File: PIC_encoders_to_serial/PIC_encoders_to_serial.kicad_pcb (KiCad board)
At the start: 4 copper layers, 35 x 35 mm, 20 parts, among them J1 Programming, J2 Conn_01x02, J3 Conn_01x04, J4 Conn_01x05, J5 Conn_01x05, U1 DSPIC33FJ64MC802-xSP, U2 LM78L33_TO92

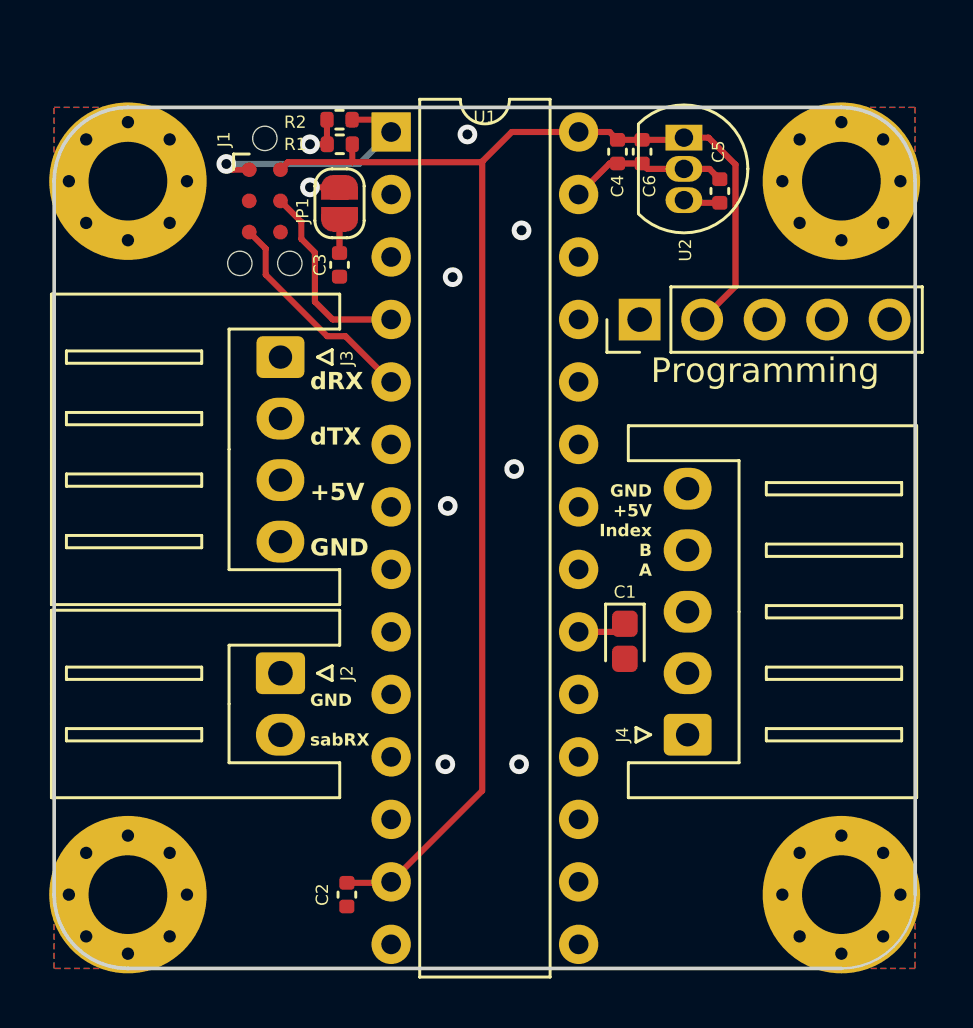
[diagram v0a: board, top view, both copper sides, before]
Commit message: changed connectors from JST XH to Molex mini-SPOX
mini-spox is smaller, but retains an almost 2.54mm pitch, so is still somewhat compatible with pin headers if need be
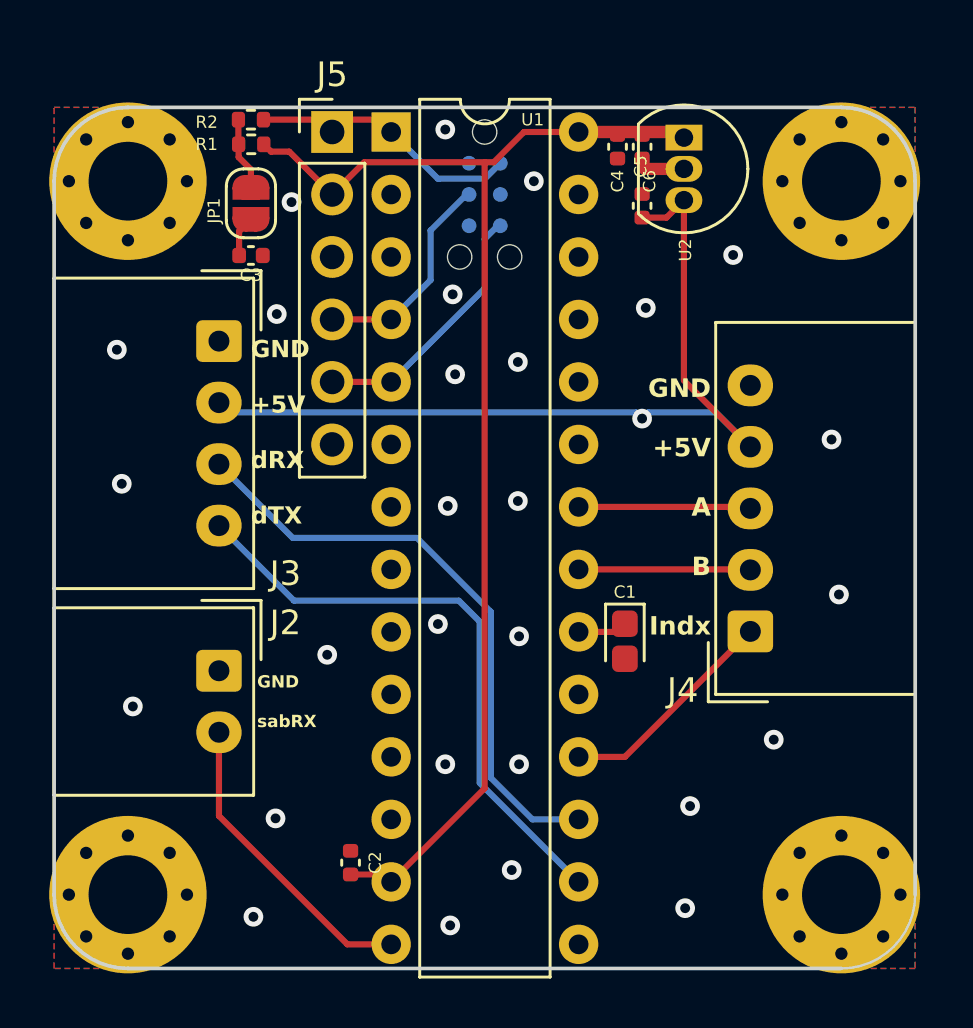
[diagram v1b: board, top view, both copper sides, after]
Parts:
- J1: moved to B.Cu
- J2: footprint Connector_JST:JST_XH_S2B-XH-A_1x02_P2.50mm_Horizontal -> Connector_Molex:Molex_SPOX_5268-02A_1x02_P2.50mm_Horizontal
- J3: footprint Connector_JST:JST_XH_S4B-XH-A_1x04_P2.50mm_Horizontal -> Connector_Molex:Molex_SPOX_5268-04A_1x04_P2.50mm_Horizontal
- J4: footprint Connector_JST:JST_XH_S5B-XH-A_1x05_P2.50mm_Horizontal -> Connector_Molex:Molex_SPOX_5268-05A_1x05_P2.50mm_Horizontal
- J5: value Conn_01x05 -> Programming; footprint Connector_PinHeader_2.54mm:PinHeader_1x05_P2.54mm_Vertical -> Connector_PinHeader_2.54mm:PinHeader_1x06_P2.54mm_Vertical
- moved J5 14.6 mm to (126.3, 56.0), turned to 0 degrees
- moved J1 8.94 mm to (132.5, 58.5)
- moved J4 4.91 mm to (143.3, 76.3)
- moved C3 3.62 mm to (123.0, 61.0), turned to 0 degrees
- moved JP1 3.60 mm to (123.0, 58.9)
- moved R1 3.60 mm to (123.0, 56.5)
- moved R2 3.60 mm to (123.0, 55.5)
- moved C5 3.22 mm to (138.9, 59.0)
- moved J3 2.58 mm to (121.7, 64.5)
- moved J2 2.50 mm to (121.7, 77.9)
- moved C2 1.31 mm to (127.0, 85.7), turned to 90 degrees
- moved C4 0.20 mm to (137.9, 56.6)
- moved C6 0.20 mm to (138.9, 56.6)
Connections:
- J3 pad 1: /pic_RX -> GND
- J3 pad 2: /pic_TX -> +5V
- J3 pad 3: +5V -> /pic_RX
- J3 pad 4: GND -> /pic_TX
- J4 pad 1: /QEI_A -> /QEI_I
- J4 pad 3: /QEI_I -> /QEI_A
- U1 pad 14: unconnected-(U1-PGED3/ASDA1/RP5/CN27/PMD7/RB5-Pad14) -> /Saber_RX
- U1 pad 15: /QEI_A -> unconnected-(U1-PGEC3/ASCL1/RP6/CN24/PMD6/RB6-Pad15)
- U1 pad 16: /QEI_B -> /pic_TX
- U1 pad 17: /QEI_I -> /pic_RX
- U1 pad 18: /Saber_RX -> /QEI_I
- U1 pad 21: /pic_TX -> /QEI_B
- U1 pad 22: /pic_RX -> /QEI_A
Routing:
- net /PGD_5: track 31.3 -> 10.5 mm
- net /PGD_4: track 26.9 -> 8.75 mm
- net /~{MCLR}: track 23.3 -> 10.9 mm, vias 1 -> 0
- net /pic_RX: track 14.6 -> 24.6 mm
- net /pic_TX: track 14.7 -> 24.5 mm
- net +3.3V: track 60.0 -> 51.7 mm
- net GND: track 6.53 -> 1.60 mm, vias 7 -> 28
- net /QEI_A: track 10.4 -> 7.00 mm
- net /QEI_B: track 10.3 -> 6.99 mm
- net Net-(JP1-B): track 4.65 -> 2.96 mm, vias 2 -> 0
- net /QEI_I: track 10.3 -> 9.09 mm
- net +5V: track 36.7 -> 35.7 mm, vias 0 -> 1
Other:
- copper layers 4 -> 2
- board text added: "GND +5V A B Indx"
- board text added: "GND +5V dRX dTX"
- board text removed: "GND +5V Index B A"
- board text removed: "dRX dTX +5V GND"
